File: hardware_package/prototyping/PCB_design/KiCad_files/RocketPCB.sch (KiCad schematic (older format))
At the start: 47 parts

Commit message: Updated PCB schematics
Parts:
- added BT?: Battery_Cell, symbol Device:Battery_Cell
- added D?: D, symbol Device:D
- added R? (x3): 10k, symbol Device:R
- added U?: MPU-6050, QFN50P400X400X95-24N, symbol MPU-6050:MPU-6050
- added U?: RFM69HCW, symbol RF_AM_FM:RFM69HCW
- added X?: GPS_PA1010D, symbol gps_pa1010d:GPS_PA1010D
- Q?: symbol Transistor_FET:DMG2301L -> RocketPCB-rescue:DMG2301L-Transistor_FET
- U?: symbol W25Q16BVSSIG:W25Q16BVSSIG -> RocketPCB-rescue:W25Q16BVSSIG-W25Q16BVSSIG
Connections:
- net labels added: 1PPS, ANT, RXI, SCL, TX0, VBACKUP, WAKEUP, ~Reset~
- net labels removed: TP1, TP2
- wire segments 230 -> 255
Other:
- note added: "GPS MODULE\n"
- note added: "IMU\n"
- note added: "Radio Module"
- moved on the sheet: C?, D?, FB?, J?, R?, U?, Y?

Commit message: Setting up IMUs
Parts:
- added C?: 10uF, symbol Device:C
- added C?: 0.1u, symbol Device:C
- added C?: 2.2u, symbol Device:C
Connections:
- net labels added: CLKIN, CS_3V, DIO0, DIO1, DIO2, DIO3, DIO4, DIO5, FSYNC_IN, INT, MISO_3V, MOSI_3V, RST_3V, SCK_3V, SCL_3V, SDA_3V
- wire segments 255 -> 291

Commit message: Minor changes
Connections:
- net labels added: AD0, SCL_EXT, SDA_EXT
- wire segments 291 -> 292
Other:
- note added: "STM32F405 MicroProcessor\n"
- note removed: "ADAFRUIT FEATHER\n"
- moved on the sheet: C?, D?, FB?, R?, U?, Y?

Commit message: fixing values, connecting nets and removing redundant nets
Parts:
- removed C?: 10uF, symbol Device:C
- removed D?: LED, symbol Device:LED
- removed J?: SD_Card, symbol Connector:SD_Card
- removed Q?: Q_PMOS_DGS, symbol Device:Q_PMOS_DGS
- removed R?: 5.1k, symbol Device:R
- removed R?: 1k, symbol Device:R
- removed U?: MCP73831-2-OT, Package_TO_SOT_SMD:SOT-23-5, symbol Battery_Management:MCP73831-2-OT
- added D?: LED, symbol Device:LED
- added J?: Micro_SD_Card, symbol Connector:Micro_SD_Card
- added R?: 2.2k, symbol Device:R
- added R?: 10k, symbol Device:R
- added R?: 100k, symbol Device:R
- R?: value 100k -> 10k
- R?: value R -> 10k
- U?: symbol MPU-6050:MPU-6050 -> RocketPCB-rescue:MPU-6050-MPU-6050
- U?: symbol RF_AM_FM:RFM69HCW -> RocketPCB-rescue:RFM69HCW-RF_AM_FM
- X?: symbol gps_pa1010d:GPS_PA1010D -> RocketPCB-rescue:GPS_PA1010D-gps_pa1010d
- Y?: value 32.768 -> 12MHz
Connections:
- net labels added: +3V8, CS, TP3
- net labels removed: +7.5V, CS_3V, D8_NEOPIX, MISO_3V, MOSI_3V, RESET, RST_3V, SCI, SCK_3V, SCL_3V, SDA_3V
- wire segments 292 -> 274
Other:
- note added: "I2C1"
- note removed: "Battery Charger\n"
- note removed: "J2C1\n"
- note removed: "SD card reader/writer"

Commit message: Completed Schematic
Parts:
- added C? (x2): 100nF, symbol Device:C
- added C?: 10uF, symbol Device:C
- added SW?: SW_Push, symbol Switch:SW_Push
- added U?: MPL3115A2, Package_LGA:NXP_LGA-8_3x5mm_P1.25mm_H1.1mm, symbol Sensor_Pressure:MPL3115A2
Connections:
- net labels added: INT1, INT2
- net labels removed: AD0, SCL_EXT, SDA_EXT
- wire segments 274 -> 290
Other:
- note added: "Barometer\n"
- note added: "Program"
- note added: "microSD card port"
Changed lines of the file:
@@
 Wire Wire Line
 	10300 2100 9850 2100
-Wire Wire Line
-	10300 2300 9850 2300
-Wire Wire Line
-	10300 1400 9850 1400
 Text Label 9900 2000 0    59   ~ 0
 SCL
 Text Label 9900 2100 0    59   ~ 0
 SDA
-Wire Wire Line
-	10300 1500 9850 1500
-Text Label 9950 1500 0    59   ~ 0
-AD0
-Text Label 9900 2300 0    59   ~ 0
-SDA_EXT
-Text Label 9900 1400 0    59   ~ 0
-SCL_EXT
 Wire Notes Line
 	12650 2200 16050 2200
@@
 Text Label 7750 3700 0    50   ~ 0
 CS
+$Comp
+L power:GND #PWR?
+U 1 1 5F6AE296
+P 9850 1800
+F 0 "#PWR?" H 9850 1550 50  0001 C CNN
+F 1 "GND" H 9855 1627 50  0000 C CNN
+F 2 "" H 9850 1800 50  0001 C CNN
+F 3 "" H 9850 1800 50  0001 C CNN
+	1    9850 1800
+	0    1    1    0
+$EndComp
+$Comp
+L power:GND #PWR?
+U 1 1 5F6AEB87
+P 9850 1300
+F 0 "#PWR?" H 9850 1050 50  0001 C CNN
+F 1 "GND" H 9855 1127 50  0000 C CNN
+F 2 "" H 9850 1300 50  0001 C CNN
+F 3 "" H 9850 1300 50  0001 C CNN
+	1    9850 1300
+	0    1    1    0
+$EndComp
+Wire Notes Line
+	450  8600 3950 8600
+Wire Notes Line
+	3950 8600 3950 11200
+Text Notes 550  8750 0    71   ~ 0
+microSD card port
+$Comp
+L Sensor_Pressure:MPL3115A2 U?
+U 1 1 5F6F2546
+P 14400 6400
+F 0 "U?" H 14050 5900 50  0000 C CNN
+F 1 "MPL3115A2" H 14050 5800 50  0000 C CNN
+F 2 "Package_LGA:NXP_LGA-8_3x5mm_P1.25mm_H1.1mm" H 15400 5950 50  0001 C CNN
+F 3 "https://www.nxp.com/docs/en/data-sheet/MPL3115A2.pdf" H 14400 6400 50  0001 C CNN
+	1    14400 6400
+	1    0    0    -1
+$EndComp
+Wire Wire Line
+	14400 5750 14400 5900
+Wire Wire Line
+	14000 6400 13600 6400
+Wire Wire Line
+	14000 6300 13600 6300
+Text Label 13700 6300 0    71   ~ 0
+SDA
+Text Label 13700 6400 0    71   ~ 0
+SCL
+Wire Wire Line
+	14400 6900 14400 7050
+$Comp
+L power:GND #PWR?
+U 1 1 5F76D8E9
+P 14400 7050
+F 0 "#PWR?" H 14400 6800 50  0001 C CNN
+F 1 "GND" H 14405 6877 50  0000 C CNN
+F 2 "" H 14400 7050 50  0001 C CNN
+F 3 "" H 14400 7050 50  0001 C CNN
+	1    14400 7050
+	1    0    0    -1
+$EndComp
+Wire Wire Line
+	14800 6600 15050 6600
+Wire Wire Line
+	15050 6600 15050 6800
+$Comp
+L Device:C C?
+U 1 1 5F78545C
+P 15050 6950
+F 0 "C?" H 15165 6996 50  0000 L CNN
+F 1 "100nF" H 15165 6905 50  0000 L CNN
+F 2 "" H 15088 6800 50  0001 C CNN
+F 3 "~" H 15050 6950 50  0001 C CNN
+	1    15050 6950
+	1    0    0    -1
+$EndComp
+$Comp
+L power:GND #PWR?
+U 1 1 5F785A3F
+P 15050 7100
+F 0 "#PWR?" H 15050 6850 50  0001 C CNN
+F 1 "GND" H 15055 6927 50  0000 C CNN
+F 2 "" H 15050 7100 50  0001 C CNN
+F 3 "" H 15050 7100 50  0001 C CNN
+	1    15050 7100
+	1    0    0    -1
+$EndComp
+$Comp
+L Device:C C?
+U 1 1 5F786096
+P 13650 5800
+F 0 "C?" H 13765 5846 50  0000 L CNN
+F 1 "100nF" H 13765 5755 50  0000 L CNN
+F 2 "" H 13688 5650 50  0001 C CNN
+F 3 "~" H 13650 5800 50  0001 C CNN
+	1    13650 5800
+	1    0    0    -1
+$EndComp
+$Comp
+L Device:C C?
+U 1 1 5F787168
+P 13200 5800
+F 0 "C?" H 13315 5846 50  0000 L CNN
+F 1 "10uF" H 13315 5755 50  0000 L CNN
+F 2 "" H 13238 5650 50  0001 C CNN
+F 3 "~" H 13200 5800 50  0001 C CNN
+	1    13200 5800
+	1    0    0    -1
+$EndComp
+Wire Wire Line
+	14300 5500 13650 5500
+Wire Wire Line
+	13650 5500 13650 5650
+Wire Wire Line
+	14300 5500 14300 5900
+Wire Wire Line
+	13650 5500 13200 5500
+Wire Wire Line
+	13200 5500 13200 5650
+Connection ~ 13650 5500
+Wire Wire Line
+	13200 5950 13200 6050
+Wire Wire Line
+	13200 6050 13650 6050
+Wire Wire Line
+	13650 6050 13650 5950
+Wire Wire Line
+	13200 6050 13200 6150
+Connection ~ 13200 6050
+$Comp
+L power:GND #PWR?
+U 1 1 5F7E572C
+P 13200 6150
+F 0 "#PWR?" H 13200 5900 50  0001 C CNN
+F 1 "GND" H 13205 5977 50  0000 C CNN
+F 2 "" H 13200 6150 50  0001 C CNN
+F 3 "" H 13200 6150 50  0001 C CNN
+	1    13200 6150
+	1    0    0    -1
+$EndComp
+$Comp
+L power:+3.3V #PWR?
+U 1 1 5F7E5CFF
+P 14300 5500
+F 0 "#PWR?" H 14300 5350 50  0001 C CNN
+F 1 "+3.3V" H 14315 5673 50  0000 C CNN
+F 2 "" H 14300 5500 50  0001 C CNN
+F 3 "" H 14300 5500 50  0001 C CNN
+	1    14300 5500
+	1    0    0    -1
+$EndComp
+Connection ~ 14300 5500
+$Comp
+L power:+3.3V #PWR?
+U 1 1 5F7E66C7
+P 14400 5750
+F 0 "#PWR?" H 14400 5600 50  0001 C CNN
+F 1 "+3.3V" H 14415 5923 50  0000 C CNN
+F 2 "" H 14400 5750 50  0001 C CNN
+F 3 "" H 14400 5750 50  0001 C CNN
+	1    14400 5750
+	1    0    0    -1
+$EndComp
+Wire Wire Line
+	14800 6300 15250 6300
+Wire Wire Line
+	14800 6400 15250 6400
+Text Label 14900 6300 0    71   ~ 0
+INT1
+Text Label 14900 6400 0    71   ~ 0
+INT2
+Text Notes 12750 5150 0    71   ~ 0
+Barometer\n
+$Comp
+L Switch:SW_Push SW?
+U 1 1 5F878647
+P 1350 4900
+F 0 "SW?" H 1350 5185 50  0000 C CNN
+F 1 "SW_Push" H 1350 5094 50  0000 C CNN
+F 2 "" H 1350 5100 50  0001 C CNN
+F 3 "~" H 1350 5100 50  0001 C CNN
+	1    1350 4900
+	1    0    0    -1
+$EndComp
+Wire Wire Line
+	1550 4900 1900 4900
+Wire Wire Line
+	1150 4900 800  4900
+$Comp
+L power:GND #PWR?
+U 1 1 5F8C15A9
+P 800 4900
+F 0 "#PWR?" H 800 4650 50  0001 C CNN
+F 1 "GND" V 805 4772 50  0000 R CNN
+F 2 "" H 800 4900 50  0001 C CNN
+F 3 "" H 800 4900 50  0001 C CNN
+	1    800  4900
+	0    1    1    0
+$EndComp
+Text Label 1550 4900 0    71   ~ 0
+BOOT0
+Text Notes 1150 5050 0    71   ~ 0
+Program
 $EndSCHEMATC

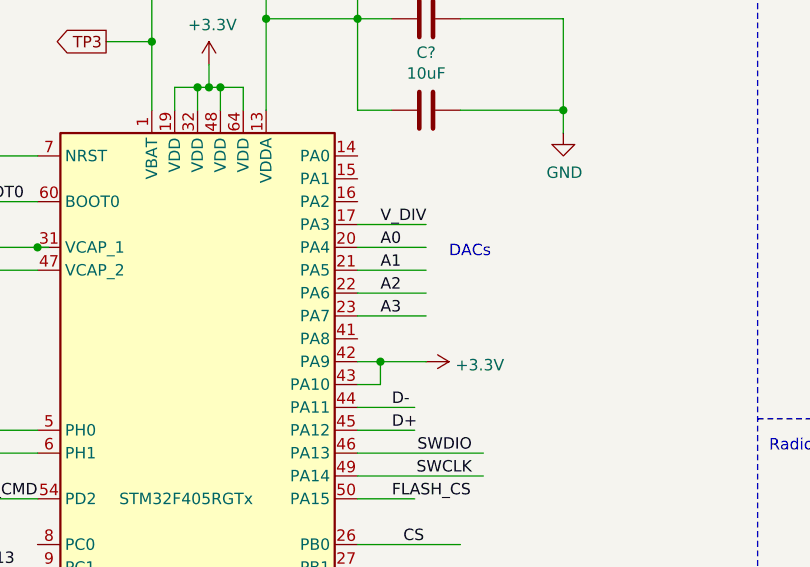
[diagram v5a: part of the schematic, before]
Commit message: Edit Wired interrupts to STM pins
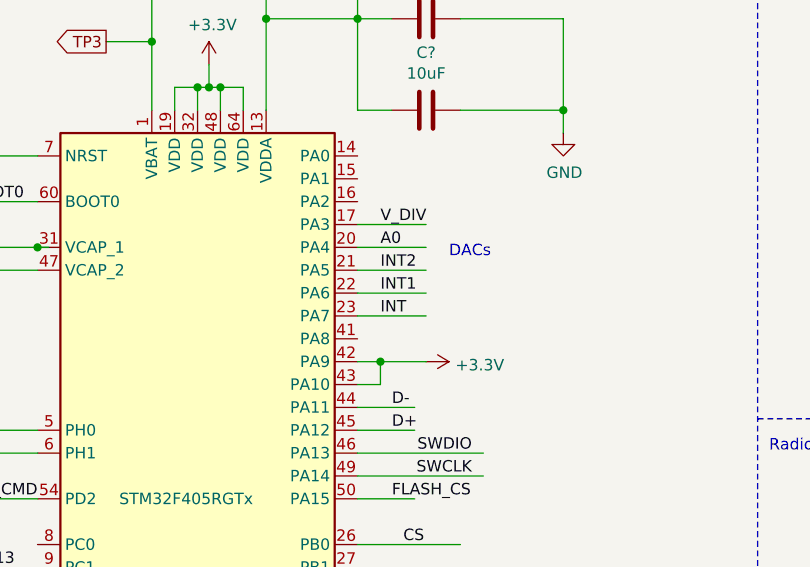
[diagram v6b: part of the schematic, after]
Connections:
- net labels removed: A1, A2, A3
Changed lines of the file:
@@
 A0
 Text Label 7650 2500 0    50   ~ 0
-A1
+INT2
 Text Label 7650 2600 0    50   ~ 0
-A2
+INT1
 Text Notes 7950 2450 0    50   ~ 0
 DACs
@@
 	7650 2900 7650 3000
 Text Label 7650 2700 0    50   ~ 0
-A3
+INT
 Wire Wire Line
 	6850 5500 6950 5500

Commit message: Editied titles and boundaries to tidy up layout
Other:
- note added: "Reset & Prog Switches\n"
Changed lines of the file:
@@
 Text Notes 12850 2900 3    50   ~ 0
 Voltage Divider
-Text Notes 800  1400 3    50   ~ 0
+Text Notes 2750 650  0    71   ~ 0
 USB-C Connector\n
 Text Notes 13250 10950 2    59   ~ 12
@@
 Text Notes 1150 5050 0    71   ~ 0
 Program
+Wire Notes Line
+	450  5250 3850 5250
+Text Notes 2500 3950 0    71   ~ 0
+Reset & Prog Switches\n
 $EndSCHEMATC

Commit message: Added Battery Regulator
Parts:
- added C?: 22uF, symbol Device:C
- added C?: 10uF, symbol Device:C
- added L?: 2.2uH, symbol Device:L
- added R?: 649k, symbol Device:R
- added R?: 180k, symbol Device:R
- added R?: 100k, symbol Device:R
- added U?: TPS62160DSG, Package_SON:WSON-8-1EP_2x2mm_P0.5mm_EP0.9x1.6mm_ThermalVias, symbol Regulator_Switching:TPS62160DSG
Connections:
- net labels added: +7.5V, PG
- net labels removed: +3V8
- wire segments 290 -> 324
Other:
- note added: "Battery Regulator\n"
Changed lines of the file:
@@
 	-1   0    0    1
 $EndComp
-$Comp
-L power:+BATT #PWR?
-U 1 1 5F51DC94
-P 15200 3150
-F 0 "#PWR?" H 15200 3000 50  0001 C CNN
-F 1 "+BATT" V 15215 3278 50  0000 L CNN
-F 2 "" H 15200 3150 50  0001 C CNN
-F 3 "" H 15200 3150 50  0001 C CNN
-	1    15200 3150
-	0    1    1    0
-$EndComp
-Wire Wire Line
-	14800 3150 15200 3150
 Wire Wire Line
 	14800 3250 14950 3250
@@
 	12650 500  12650 8050
 Wire Notes Line
-	9300 8050 16050 8050
-Wire Notes Line
 	9300 450  9300 8050
 Text Label 13150 3150 0    50   ~ 0
@@
 Wire Wire Line
 	14800 3050 15250 3050
-$Comp
-L power:+3V8 #PWR?
-U 1 1 5F95B0D5
-P 15250 3050
-F 0 "#PWR?" H 15250 2900 50  0001 C CNN
-F 1 "+3V8" V 15265 3178 50  0000 L CNN
-F 2 "" H 15250 3050 50  0001 C CNN
-F 3 "" H 15250 3050 50  0001 C CNN
-	1    15250 3050
-	0    1    1    0
-$EndComp
 Wire Wire Line
 	7550 3700 8000 3700
@@
 Text Notes 2500 3950 0    71   ~ 0
 Reset & Prog Switches\n
+$Comp
+L Regulator_Switching:TPS62160DSG U?
+U 1 1 5F72D5C8
+P 9350 9750
+F 0 "U?" H 9350 10317 50  0000 C CNN
+F 1 "TPS62160DSG" H 9350 10226 50  0000 C CNN
+F 2 "Package_SON:WSON-8-1EP_2x2mm_P0.5mm_EP0.9x1.6mm_ThermalVias" H 9500 9400 50  0001 L CNN
+F 3 "http://www.ti.com/lit/ds/symlink/tps62160.pdf" H 9350 10300 50  0001 C CNN
+	1    9350 9750
+	1    0    0    -1
+$EndComp
+$Comp
+L power:+7.5V #PWR?
+U 1 1 5F74C0CF
+P 15250 3050
+F 0 "#PWR?" H 15250 2900 50  0001 C CNN
+F 1 "+7.5V" V 15265 3178 50  0000 L CNN
+F 2 "" H 15250 3050 50  0001 C CNN
+F 3 "" H 15250 3050 50  0001 C CNN
+	1    15250 3050
+	0    1    1    0
+$EndComp
+$Comp
+L power:+7.5V #PWR?
+U 1 1 5F7502B8
+P 8350 9450
+F 0 "#PWR?" H 8350 9300 50  0001 C CNN
+F 1 "+7.5V" V 8365 9578 50  0000 L CNN
+F 2 "" H 8350 9450 50  0001 C CNN
+F 3 "" H 8350 9450 50  0001 C CNN
+	1    8350 9450
+	0    -1   -1   0
+$EndComp
+Wire Wire Line
+	8350 9450 8450 9450
+Wire Wire Line
+	8950 9550 8750 9550
+Wire Wire Line
+	8750 9550 8750 9450
+Connection ~ 8750 9450
+Wire Wire Line
+	8750 9450 8950 9450
+$Comp
+L Device:L L?
+U 1 1 5F7CC9EF
+P 10050 9450
+F 0 "L?" V 10240 9450 50  0000 C CNN
+F 1 "2.2uH" V 10149 9450 50  0000 C CNN
+F 2 "" H 10050 9450 50  0001 C CNN
+F 3 "~" H 10050 9450 50  0001 C CNN
+	1    10050 9450
+	0    -1   -1   0
+$EndComp
+Wire Wire Line
+	9750 9450 9900 9450
+Wire Wire Line
+	9750 9550 10300 9550
+Wire Wire Line
+	10300 9550 10300 9450
+Wire Wire Line
+	10300 9450 10200 9450
+$Comp
+L Device:R R?
+U 1 1 5F8016AA
+P 10300 9700
+F 0 "R?" H 10370 9746 50  0000 L CNN
+F 1 "649k" H 10370 9655 50  0000 L CNN
+F 2 "" V 10230 9700 50  0001 C CNN
+F 3 "~" H 10300 9700 50  0001 C CNN
+	1    10300 9700
+	1    0    0    -1
+$EndComp
+Connection ~ 10300 9550
+Wire Wire Line
+	10300 9850 10300 9950
+Wire Wire Line
+	10300 9950 9900 9950
+Wire Wire Line
+	9900 9950 9900 9650
+Wire Wire Line
+	9900 9650 9750 9650
+Wire Wire Line
+	10300 9950 10300 10050
+Connection ~ 10300 9950
+$Comp
+L Device:R R?
+U 1 1 5F8384B0
+P 10300 10200
+F 0 "R?" H 10370 10246 50  0000 L CNN
+F 1 "180k" H 10370 10155 50  0000 L CNN
+F 2 "" V 10230 10200 50  0001 C CNN
+F 3 "~" H 10300 10200 50  0001 C CNN
+	1    10300 10200
+	1    0    0    -1
+$EndComp
+Wire Wire Line
+	10300 10350 10300 10450
+Wire Wire Line
+	10300 10450 9450 10450
+Wire Wire Line
+	10300 9450 10700 9450
+Wire Wire Line
+	10700 9450 10700 9950
+Connection ~ 10300 9450
+$Comp
+L Device:C C?
+U 1 1 5F8702D4
+P 10700 10100
+F 0 "C?" H 10815 10146 50  0000 L CNN
+F 1 "22uF" H 10815 10055 50  0000 L CNN
+F 2 "" H 10738 9950 50  0001 C CNN
+F 3 "~" H 10700 10100 50  0001 C CNN
+	1    10700 10100
+	1    0    0    -1
+$EndComp
+Wire Wire Line
+	10700 10250 10700 10450
+Wire Wire Line
+	10700 10450 10300 10450
+Connection ~ 10300 10450
+Wire Wire Line
+	10700 9450 10800 9450
+Connection ~ 10700 9450
+$Comp
+L Device:C C?
+U 1 1 5F8E3FA7
+P 8250 9900
+F 0 "C?" H 8365 9946 50  0000 L CNN
+F 1 "10uF" H 8365 9855 50  0000 L CNN
+F 2 "" H 8288 9750 50  0001 C CNN
+F 3 "~" H 8250 9900 50  0001 C CNN
+	1    8250 9900
+	1    0    0    -1
+$EndComp
+Wire Wire Line
+	8450 9450 8450 9600
+Wire Wire Line
+	8450 9600 8250 9600
+Wire Wire Line
+	8250 9600 8250 9750
+Connection ~ 8450 9450
+Wire Wire Line
+	8450 9450 8750 9450
+Text Label 8750 9850 0    50   ~ 0
+PG
+Wire Wire Line
+	8950 9850 8600 9850
+$Comp
+L Device:R R?
+U 1 1 5F983424
+P 10300 9200
+F 0 "R?" H 10370 9246 50  0000 L CNN
+F 1 "100k" H 10370 9155 50  0000 L CNN
+F 2 "" V 10230 9200 50  0001 C CNN
+F 3 "~" H 10300 9200 50  0001 C CNN
+	1    10300 9200
+	1    0    0    -1
+$EndComp
+Wire Wire Line
+	10300 9450 10300 9350
+Wire Wire Line
+	10300 9050 10300 8800
+Text Label 10300 8850 0    50   ~ 0
+PG
+$Comp
+L power:+BATT #PWR?
+U 1 1 5F9BFCD8
+P 10800 9450
+F 0 "#PWR?" H 10800 9300 50  0001 C CNN
+F 1 "+BATT" V 10815 9578 50  0000 L CNN
+F 2 "" H 10800 9450 50  0001 C CNN
+F 3 "" H 10800 9450 50  0001 C CNN
+	1    10800 9450
+	0    1    1    0
+$EndComp
+Wire Wire Line
+	9450 10150 9450 10450
+Wire Wire Line
+	9350 10150 9350 10450
+Wire Wire Line
+	9350 10450 9450 10450
+Connection ~ 9450 10450
+Wire Wire Line
+	9250 10150 9250 10450
+Wire Wire Line
+	9250 10450 9350 10450
+Connection ~ 9350 10450
+Wire Wire Line
+	8250 10450 9250 10450
+Wire Wire Line
+	8250 10050 8250 10450
+Connection ~ 9250 10450
+Wire Wire Line
+	9350 10450 9350 10500
+$Comp
+L power:GND #PWR?
+U 1 1 5FA693A7
+P 9350 10500
+F 0 "#PWR?" H 9350 10250 50  0001 C CNN
+F 1 "GND" V 9355 10372 50  0000 R CNN
+F 2 "" H 9350 10500 50  0001 C CNN
+F 3 "" H 9350 10500 50  0001 C CNN
+	1    9350 10500
+	1    0    0    -1
+$EndComp
+Wire Notes Line
+	7500 11250 7500 8050
+Wire Notes Line
+	7500 8050 16050 8050
+Text Notes 7600 8200 0    71   ~ 0
+Battery Regulator\n
 $EndSCHEMATC
